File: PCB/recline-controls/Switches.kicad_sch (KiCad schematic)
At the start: 0 parts

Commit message: Recline Controls
Recline Control board and human machine interface board schematic complete !
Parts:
- added J10, J11, J9: 0705550036, symbol AVR-KiCAD-Lib-Connectors:0705550036
- added J6, J7, J8: 0705530002, AVR-KiCAD-Lib-Connectors:Pin_Header_Angled_1x03_Pitch2.54mm, symbol AVR-KiCAD-Lib-Connectors:0705530002
- added R13, R14, R15, R16, R17, R18, R19, R20, R21: RC0402FR-071KL, AVR-KiCAD-Lib-Resistors:R0402, symbol AVR-KiCAD-Lib-Resistors:RC0402FR-071KL
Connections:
- new net +3.3V: R13.2, R14.2, R15.2, R16.2, R17.2, R18.2, R19.2, R20.2, R21.2
- new net BUTTON1: J9.1, R19.1
- new net BUTTON2: J10.1, R20.1
- new net BUTTON3: J11.1, R21.1
- new net GND: J10.2, J11.2, J6.2, J7.2, J8.2, J9.2
- new net ROCKER1_A: J6.1, R18.1
- new net ROCKER1_B: J6.3, R17.1
- new net ROCKER2_A: J7.1, R16.1
- new net ROCKER2_B: J7.3, R15.1
- new net ROCKER3_A: J8.1, R14.1
- new net ROCKER3_B: J8.3, R13.1

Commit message: PCB Started
PCB design for Recline Control Board started, figuring out PCB shape and connector positioning, work in progress !
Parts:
- J10, J11, J9: footprint (none) -> AVR-KiCAD-Lib-Connectors:Pin_Header_Angled_1x02_Pitch2.54mm
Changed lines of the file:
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@@
 			)
 		)
-		(property "Footprint" ""
+		(property "Footprint" "AVR-KiCAD-Lib-Connectors:Pin_Header_Angled_1x02_Pitch2.54mm"
 			(at 180.34 114.3 0)
 			(effects
@@
 			)
 		)
-		(property "Footprint" ""
+		(property "Footprint" "AVR-KiCAD-Lib-Connectors:Pin_Header_Angled_1x02_Pitch2.54mm"
 			(at 180.34 127 0)
 			(effects
@@
 			)
 		)
-		(property "Footprint" ""
+		(property "Footprint" "AVR-KiCAD-Lib-Connectors:Pin_Header_Angled_1x02_Pitch2.54mm"
 			(at 180.34 139.7 0)
 			(effects

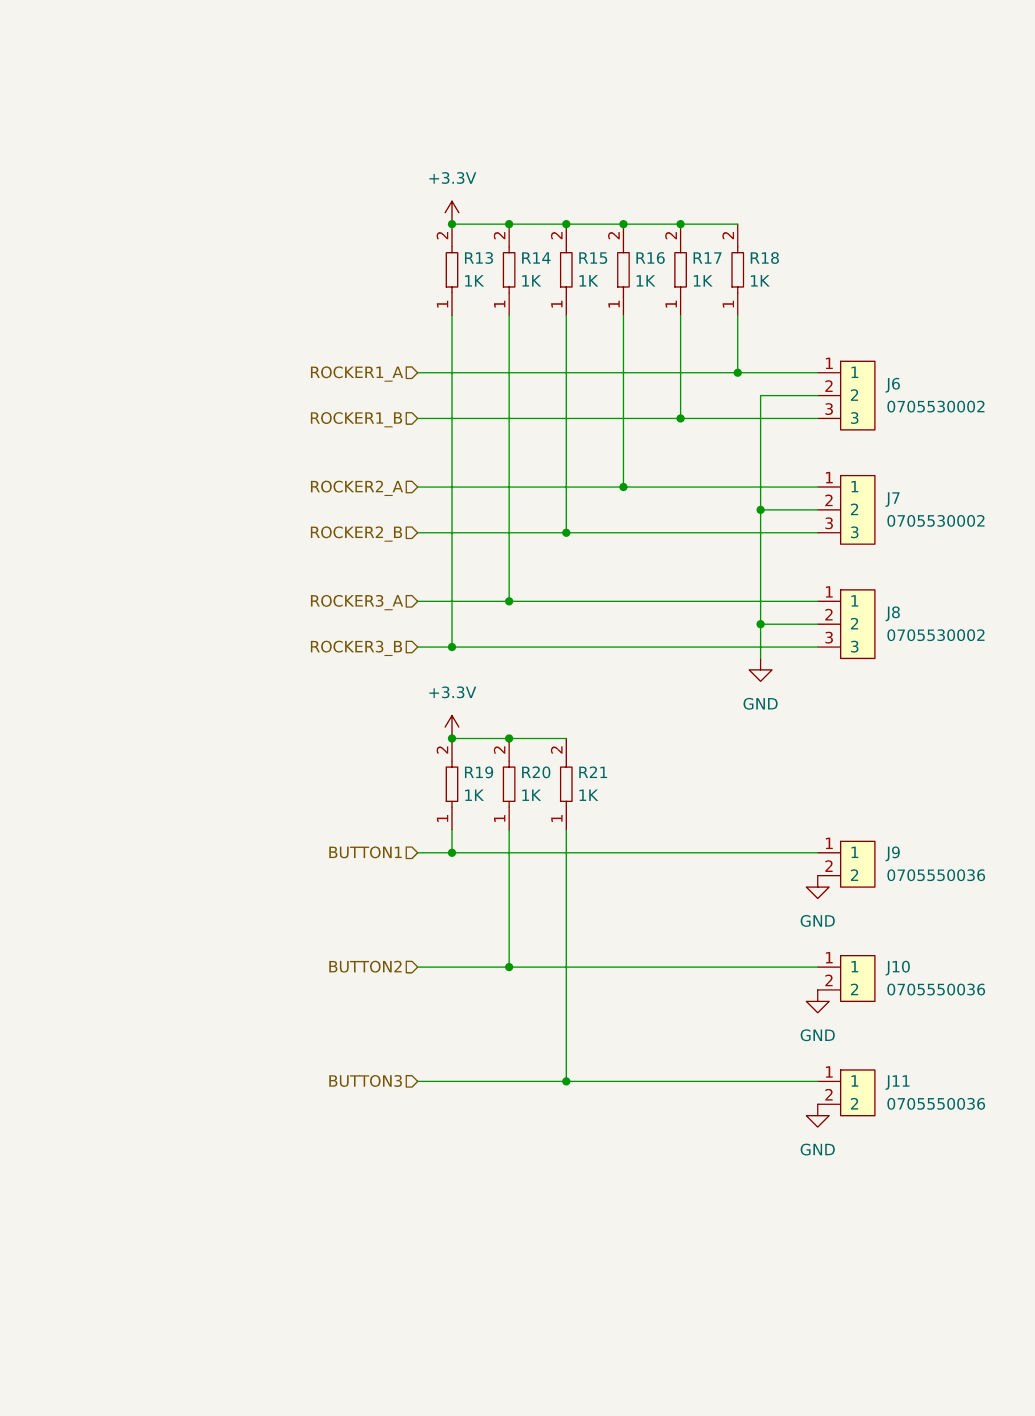
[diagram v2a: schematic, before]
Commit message: All Hardware Tweaked / 3D Renders
PCBs for Actuator Control, Recline Control HID, and 7 Segment carrier are all complete with full 3D models rendering. 3D Renders of all board added to repository img directory.
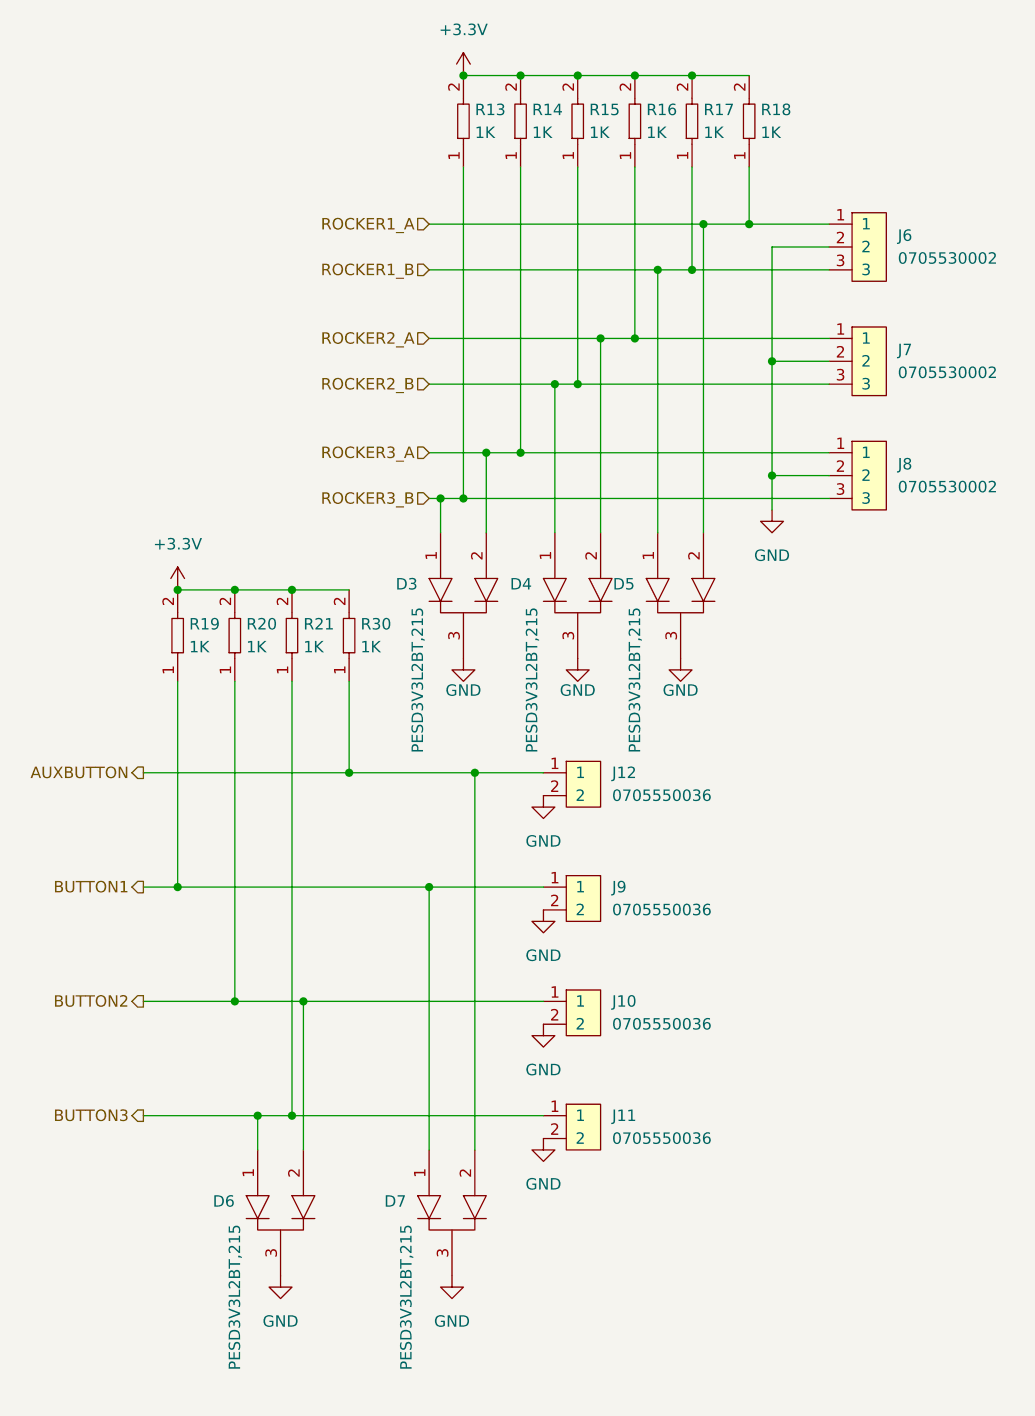
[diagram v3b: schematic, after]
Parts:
- added D3, D4, D5, D6, D7: PESD3V3L2BT,215, AVR-KiCAD-Lib-Diodes:SOT-23, symbol AVR-KiCAD-Lib-Diodes:PESD3V3L2BT,215
- added J12: 0705550036, AVR-KiCAD-Lib-Connectors:Pin_Header_Angled_1x02_Pitch2.54mm, symbol AVR-KiCAD-Lib-Connectors:0705550036
- added R30: RC0402FR-071KL, AVR-KiCAD-Lib-Resistors:R0402, symbol AVR-KiCAD-Lib-Resistors:RC0402FR-071KL
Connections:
- net +3.3V: now also R30.2
- net BUTTON1: now also D7.1
- net BUTTON2: now also D6.2
- net BUTTON3: now also D6.1
- net GND: now also D3.3, D4.3, D5.3, D6.3, D7.3, J12.2
- net ROCKER1_A: now also D5.2
- net ROCKER1_B: now also D5.1
- net ROCKER2_A: now also D4.2
- net ROCKER2_B: now also D4.1
- net ROCKER3_A: now also D3.2
- net ROCKER3_B: now also D3.1
- new net AUXBUTTON: D7.2, J12.1, R30.1
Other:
- moved on the sheet: J10, J11, J6, J7, J8, J9, R13, R14, R15, R16, R17, R18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
